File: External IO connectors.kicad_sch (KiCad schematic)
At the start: 3 parts

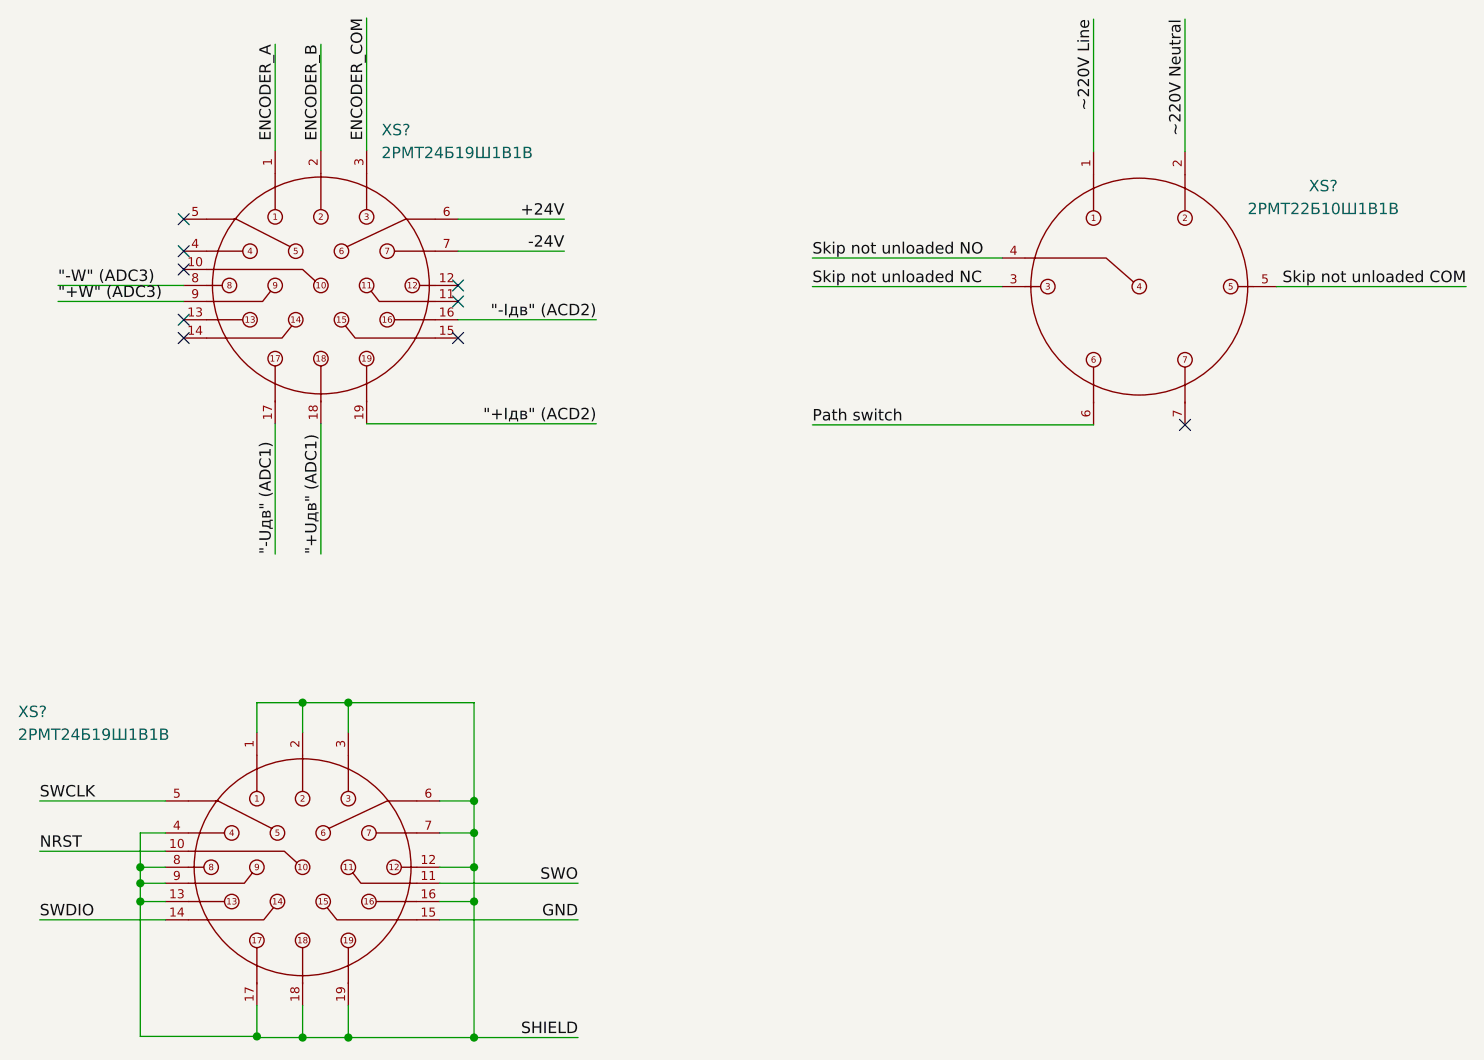
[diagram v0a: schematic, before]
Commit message: All handsolder footprints removed
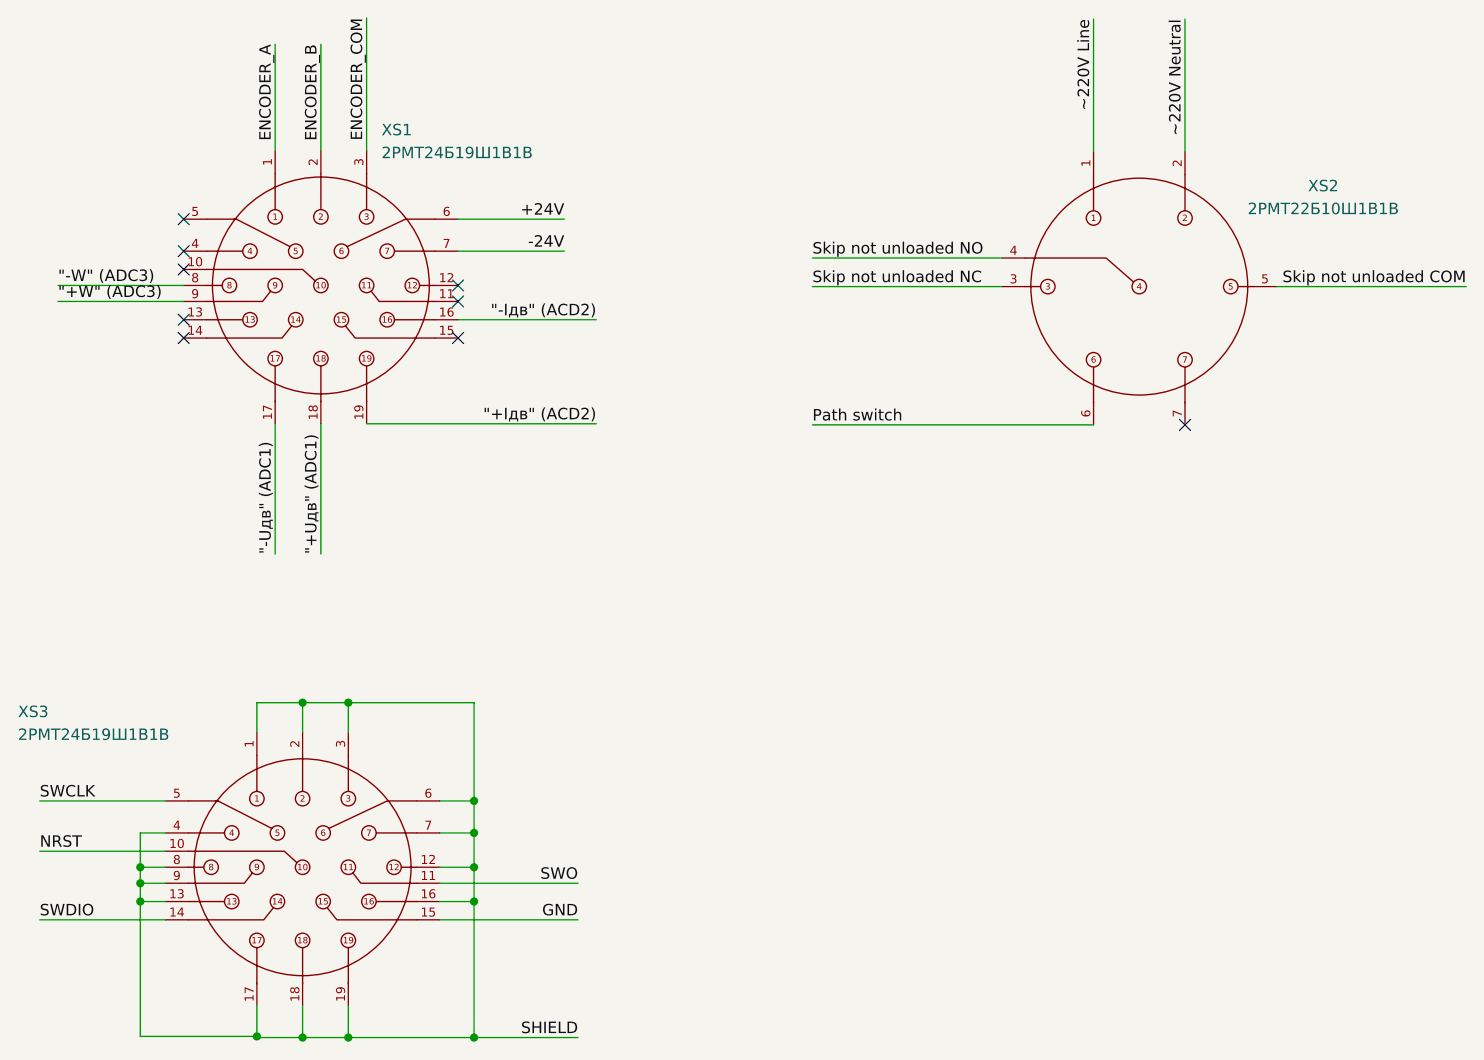
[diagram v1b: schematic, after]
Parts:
- gave numbers to parts that had none: 3
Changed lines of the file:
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@@
   (symbol (lib_id "SVIELCOM_Library:2РМТ24Б19Ш1В1В") (at 93.726 139.573 0) (unit 1)
     (in_bom no) (on_board no)
-    (property "Reference" "XS?" (id 0) (at 62.103 122.301 0)
+    (property "Reference" "XS3" (id 0) (at 62.103 122.301 0)
       (effects (font (size 1.27 1.27)) (justify left))
     )
@@
   (symbol (lib_id "SVIELCOM_Library:2РМТ22Б10Ш1В1В") (at 186.69 75.057 0) (unit 1)
     (in_bom yes) (on_board yes)
-    (property "Reference" "XS?" (id 0) (at 207.137 63.881 0))
+    (property "Reference" "XS2" (id 0) (at 207.137 63.881 0))
     (property "Value" "2РМТ22Б10Ш1В1В" (id 1) (at 207.137 66.421 0))
     (property "Footprint" "" (id 2) (at 186.69 75.057 0)
@@
   (symbol (lib_id "SVIELCOM_Library:2РМТ24Б19Ш1В1В") (at 95.758 74.93 0) (unit 1)
     (in_bom no) (on_board no) (fields_autoplaced)
-    (property "Reference" "XS?" (id 0) (at 102.4891 57.658 0)
+    (property "Reference" "XS1" (id 0) (at 102.4891 57.658 0)
       (effects (font (size 1.27 1.27)) (justify left))
     )
